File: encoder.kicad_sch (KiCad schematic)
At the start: 15 parts, among them SW1 RotaryEncoder_Switch_MP, U1 74LVC3G14

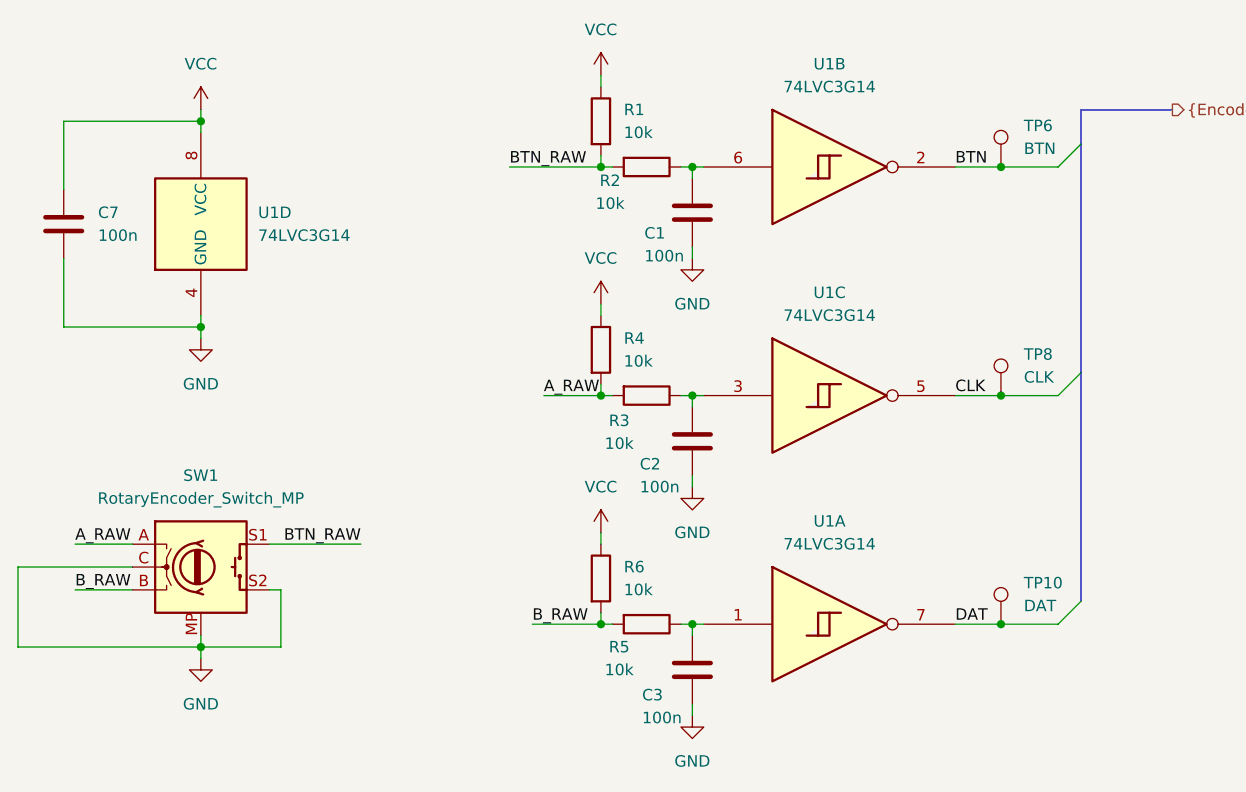
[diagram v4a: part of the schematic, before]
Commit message: Assign component LCSC part numbers
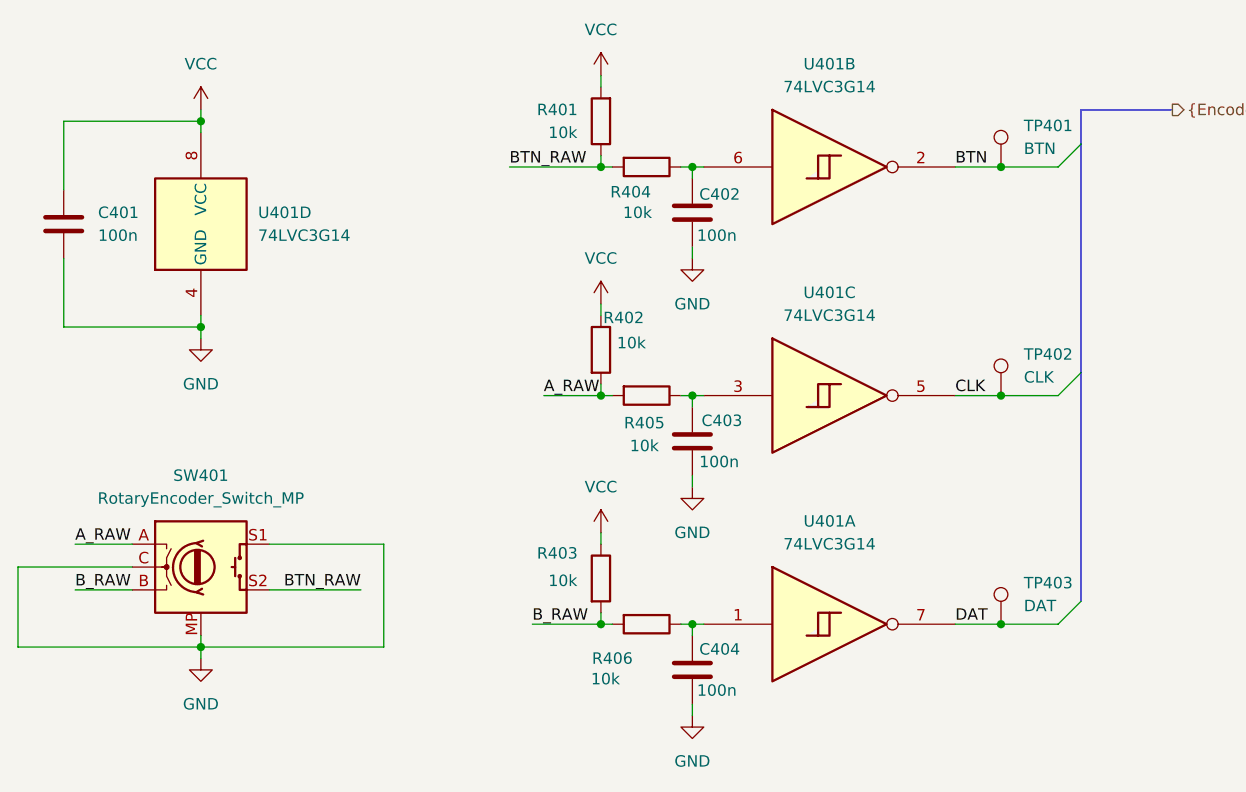
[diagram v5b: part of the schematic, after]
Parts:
- removed C1, C2, C3: 100n, Capacitor_SMD:C_1206_3216Metric_Pad1.33x1.80mm_HandSolder, symbol Device:C
- removed R1, R2, R3, R4, R5, R6: 10k, Resistor_SMD:R_1206_3216Metric_Pad1.30x1.75mm_HandSolder, symbol Device:R
- added C402, C403, C404: 100n, Capacitor_SMD:C_1206_3216Metric_Pad1.33x1.80mm_HandSolder, symbol Device:C
- added R401, R402, R403, R404, R405, R406: 10k, Resistor_SMD:R_1206_3216Metric_Pad1.30x1.75mm_HandSolder, symbol Device:R
- SW401: renamed from SW1; LCSC (none) -> C470596
- U401: renamed from U1; footprint Package_SO:SSOP-8_3.9x5.05mm_P1.27mm -> Package_SO:VSSOP-8_2.3x2mm_P0.5mm; LCSC (none) -> C98856
- renumbered C7 to C401, TP6 to TP401, TP8 to TP402, TP10 to TP403
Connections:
- net A_RAW: now also R402.2, R405.2
- net BTN_RAW: now also SW401.S2, R401.1, R404.2; no longer SW401.S1
- net B_RAW: now also R403.2, R406.2
- net GND: now also SW401.S1, C402.2, C403.2, C404.2; no longer SW401.S2
- net VCC: now also R401.2, R402.1, R403.1
- net at U401.1: now also C404.1, R406.1
- net at U401.3: now also C403.1, R405.1
- net at U401.6: now also C402.1, R404.1

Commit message: Update BOM options for export
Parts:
- C401, TP401, TP402, TP403: now left out of the parts list
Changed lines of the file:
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@@
 		(unit 1)
 		(exclude_from_sim no)
-		(in_bom yes)
+		(in_bom no)
 		(on_board yes)
 		(dnp no)
@@
 		(unit 1)
 		(exclude_from_sim no)
-		(in_bom yes)
+		(in_bom no)
 		(on_board yes)
 		(dnp no)
@@
 		(unit 1)
 		(exclude_from_sim no)
-		(in_bom yes)
+		(in_bom no)
 		(on_board yes)
 		(dnp no)
@@
 		(unit 1)
 		(exclude_from_sim no)
-		(in_bom yes)
-		(on_board yes)
-		(dnp no)
+		(in_bom no)
+		(on_board yes)
+		(dnp no)
